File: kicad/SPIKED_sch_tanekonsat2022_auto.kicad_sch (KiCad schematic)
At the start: 84 parts

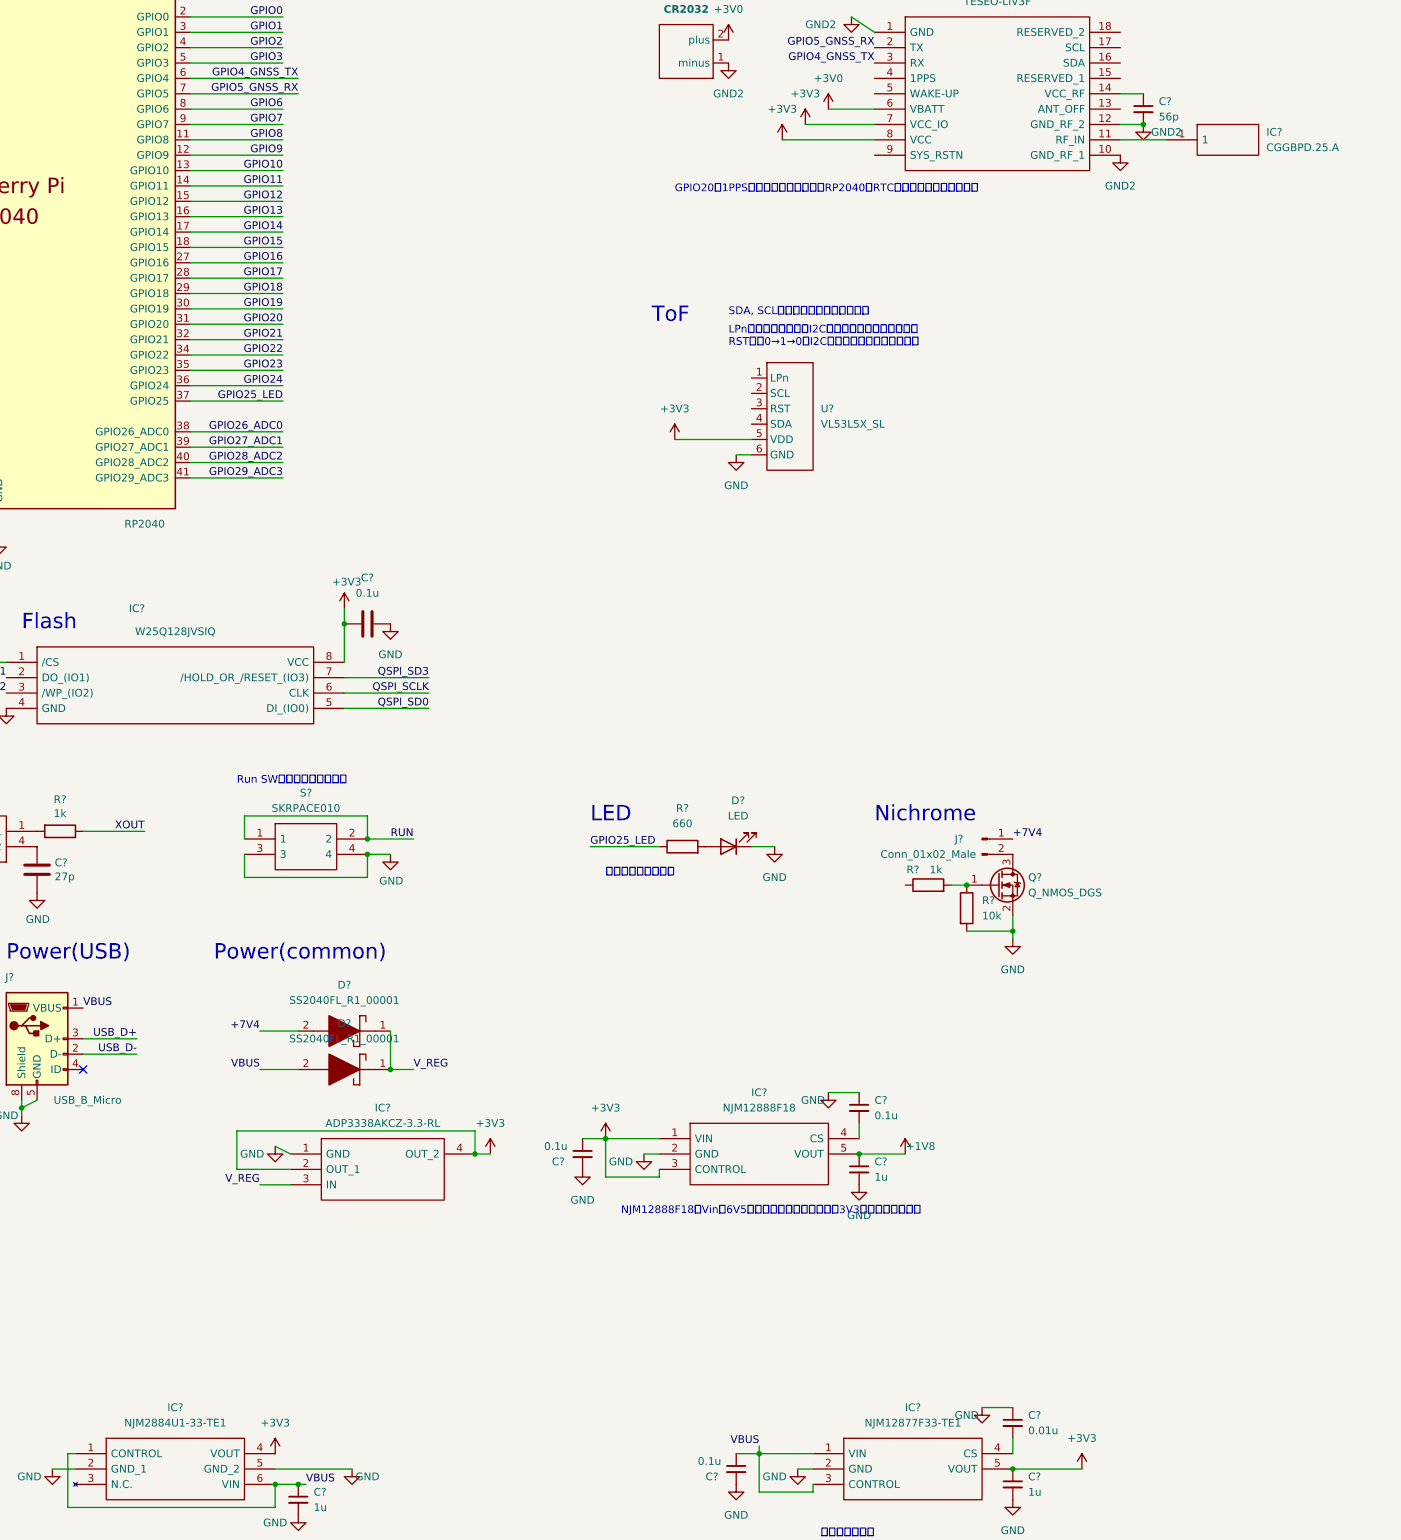
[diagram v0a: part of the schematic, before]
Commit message: update power section & interface
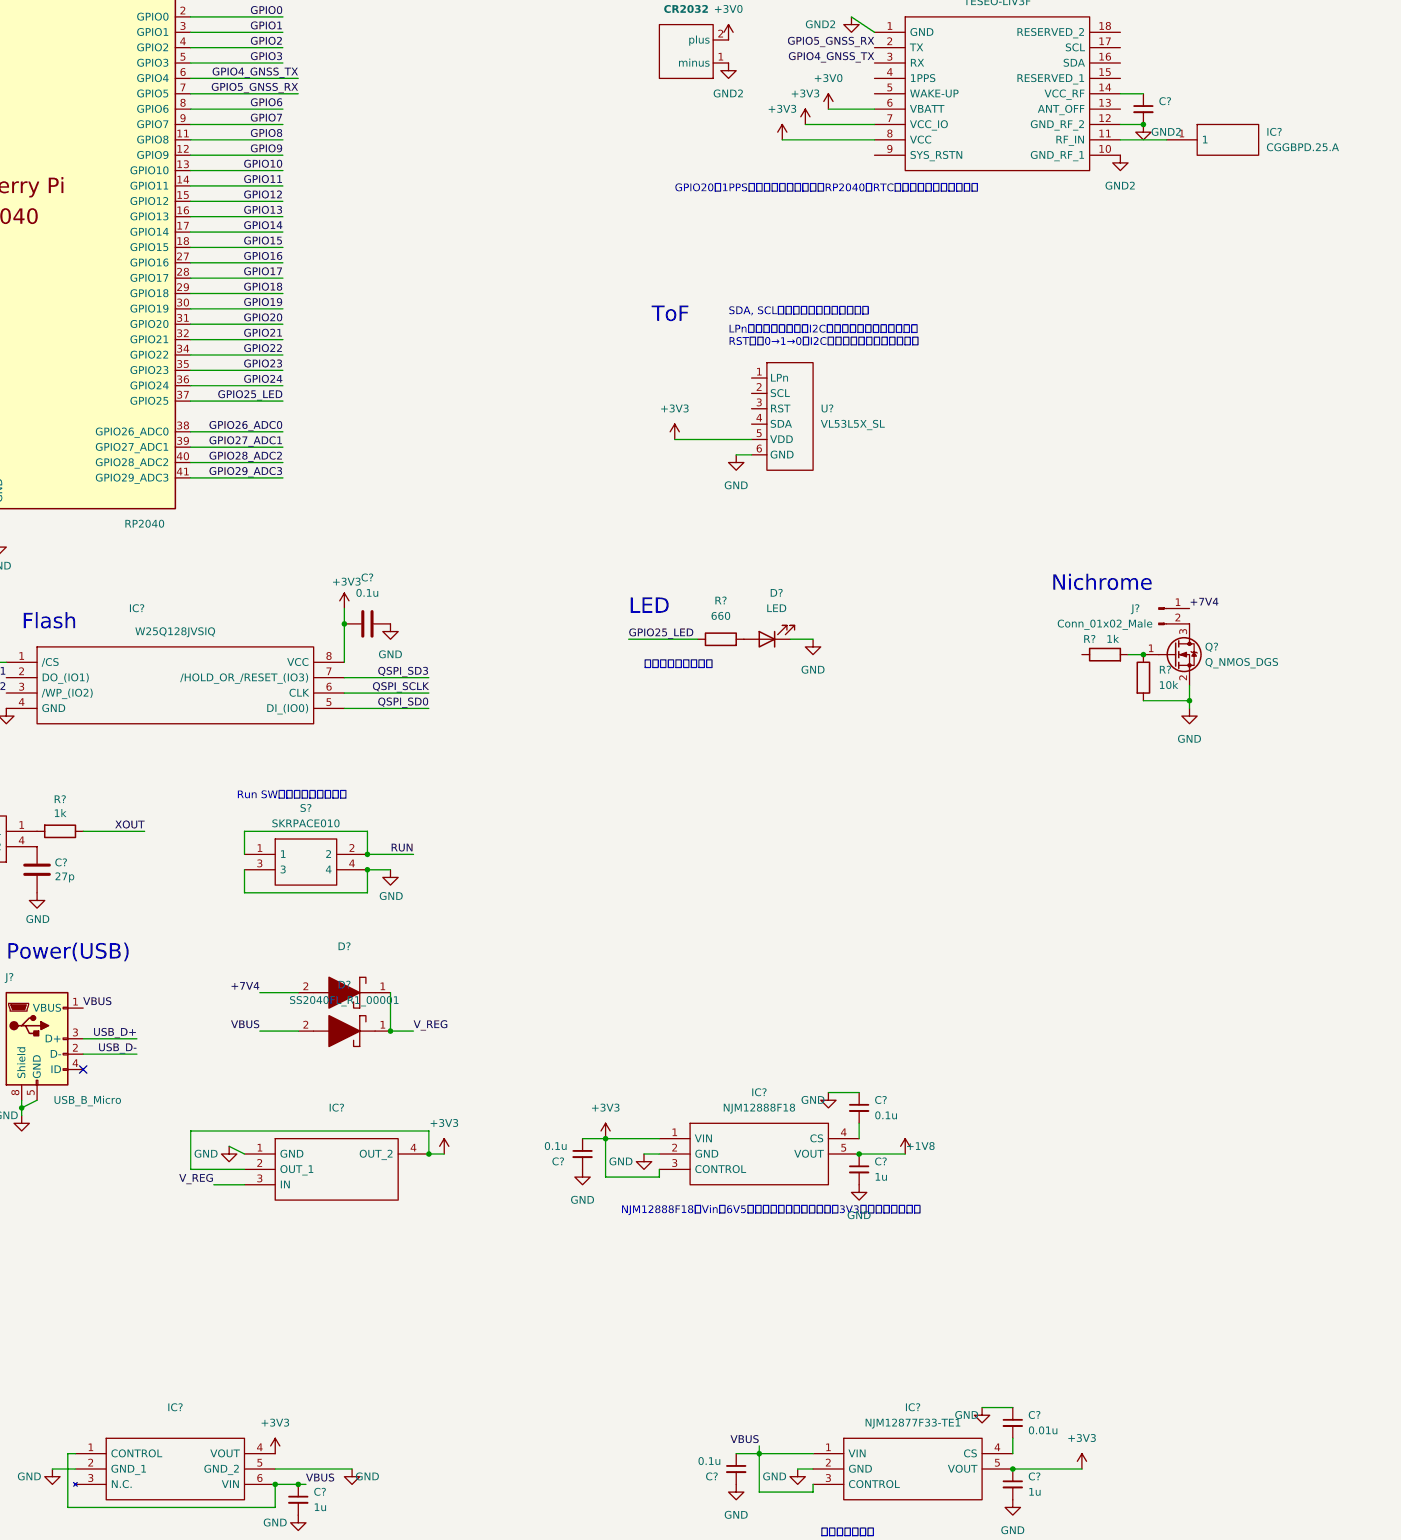
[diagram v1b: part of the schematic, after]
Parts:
- C?: value 56p -> (none)
- D?: value SS2040FL_R1_00001 -> (none); footprint SODFL3618X110N -> (none)
- IC?: value NJM2884U1-33-TE1 -> (none); footprint SOT-89-5-1 -> (none)
- IC?: value ADP3338AKCZ-3.3-RL -> (none); footprint SOT230P700X180-4N -> (none)
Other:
- note removed: "Power(common)"
- moved on the sheet: D?, IC?, J?, Q?, R?, S?
